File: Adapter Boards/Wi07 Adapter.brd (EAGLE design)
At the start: 25.4 x 24.1 mm, 5 parts, among them U1 WI07-12FULL

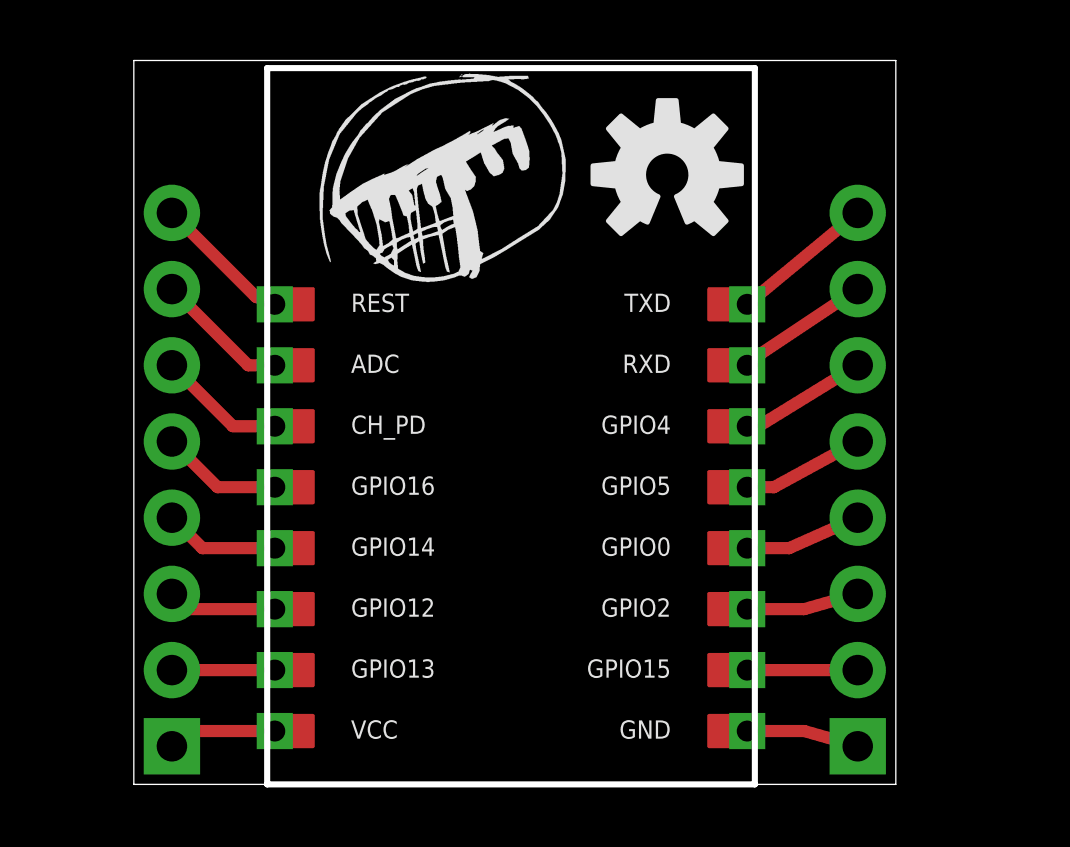
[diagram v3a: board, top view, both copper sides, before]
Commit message: Micronise hark logo; add multiple sizes
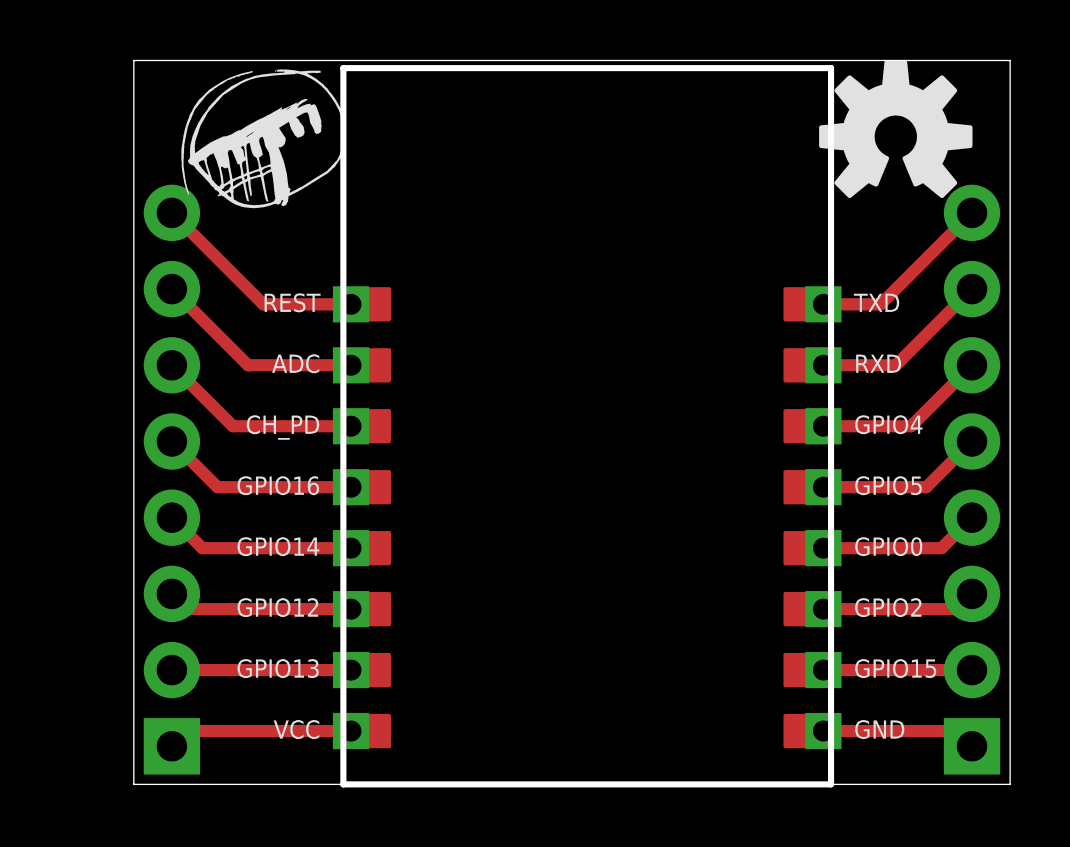
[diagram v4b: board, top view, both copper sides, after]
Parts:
- removed E$1: (no value), ESP:HARK
- added U$2: (no value), ESP:HARK-S
- moved U$1 7.73 mm to (25.4, 21.6)
- moved JP2 3.81 mm to (27.9, 1.27)
- moved U1 2.54 mm to (6.99, 0.00)
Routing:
- net N$8: track 4.64 -> 7.23 mm
- net N$3: track 3.64 -> 6.18 mm
- net N$1: track 3.64 -> 6.18 mm
- net N$7: track 4.48 -> 7.02 mm
- net N$6: track 4.27 -> 6.81 mm
- net N$5: track 4.06 -> 6.60 mm
- net N$4: track 3.85 -> 6.39 mm
- net N$2: track 3.43 -> 5.97 mm
- net N$11: track 4.26 -> 5.79 mm
- net N$12: track 4.07 -> 5.58 mm
- net N$13: track 3.90 -> 5.37 mm
- net N$9: track 4.78 -> 6.22 mm
- net N$16: track 3.75 -> 5.16 mm
- net N$14: track 3.75 -> 5.16 mm
- net N$10: track 4.71 -> 6.01 mm
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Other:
- board size 25.4 x 24.1 mm -> 29.2 x 24.1 mm
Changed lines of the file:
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@@
 <board>
 <plain>
-<wire x1="0" y1="0" x2="25.4" y2="0" width="0" layer="20"/>
-<wire x1="25.4" y1="0" x2="25.4" y2="24.13" width="0" layer="20"/>
-<wire x1="25.4" y1="24.13" x2="0" y2="24.13" width="0" layer="20"/>
+<wire x1="0" y1="0" x2="29.21" y2="0" width="0" layer="20"/>
+<wire x1="29.21" y1="0" x2="29.21" y2="24.13" width="0" layer="20"/>
+<wire x1="29.21" y1="24.13" x2="0" y2="24.13" width="0" layer="20"/>
 <wire x1="0" y1="24.13" x2="0" y2="0" width="0" layer="20"/>
 </plain>
@@
 <attribute name="VALUE" x="4.445" y="0" size="1.27" layer="27" rot="R90"/>
 </element>
-<element name="JP2" library="SparkFun-Connectors" package="1X08_PIN1_NO_SILK" value="" x="24.13" y="1.27" smashed="yes" rot="R90">
-<attribute name="NAME" x="22.3012" y="-0.0762" size="1.27" layer="27" ratio="10" rot="R90"/>
-<attribute name="VALUE" x="27.305" y="0" size="1.27" layer="27" rot="R90"/>
+<element name="JP2" library="SparkFun-Connectors" package="1X08_PIN1_NO_SILK" value="" x="27.94" y="1.27" smashed="yes" rot="R90">
+<attribute name="NAME" x="26.1112" y="-0.0762" size="1.27" layer="27" ratio="10" rot="R90"/>
+<attribute name="VALUE" x="31.115" y="0" size="1.27" layer="27" rot="R90"/>
 </element>
-<element name="U1" library="ESP" package="WI07-12" value="WI07-12FULL" x="4.445" y="0"/>
-<element name="U$1" library="SparkFun-Aesthetics" package="OSHW-LOGO-M" value="" x="17.78" y="20.32"/>
-<element name="E$1" library="ESP" package="HARK" value="" x="5.715" y="16.51"/>
+<element name="U$1" library="SparkFun-Aesthetics" package="OSHW-LOGO-M" value="" x="25.4" y="21.59"/>
+<element name="U1" library="ESP" package="WI07-12" value="WI07-12FULL" x="6.985" y="0"/>
+<element name="U$2" library="ESP" package="HARK-S" value="" x="1.27" y="19.05"/>
 </elements>
 <signals>
@@
 <contactref element="JP1" pad="1"/>
 <contactref element="U1" pad="VCC"/>
-<wire x1="4.699" y1="1.778" x2="1.778" y2="1.778" width="0.4064" layer="1"/>
+<wire x1="7.239" y1="1.778" x2="1.778" y2="1.778" width="0.4064" layer="1"/>
 <wire x1="1.778" y1="1.778" x2="1.27" y2="1.27" width="0.4064" layer="1"/>
 </signal>
@@
 <contactref element="JP1" pad="2"/>
 <contactref element="U1" pad="GPIO13"/>
-<wire x1="4.699" y1="3.81" x2="1.27" y2="3.81" width="0.4064" layer="1"/>
+<wire x1="7.239" y1="3.81" x2="1.27" y2="3.81" width="0.4064" layer="1"/>
 </signal>
 <signal name="N$3">
 <contactref element="JP1" pad="3"/>
 <contactref element="U1" pad="GPIO12"/>
-<wire x1="4.699" y1="5.842" x2="1.778" y2="5.842" width="0.4064" layer="1"/>
+<wire x1="7.239" y1="5.842" x2="1.778" y2="5.842" width="0.4064" layer="1"/>
 <wire x1="1.778" y1="5.842" x2="1.27" y2="6.35" width="0.4064" layer="1"/>
 </signal>
@@
 <contactref element="JP1" pad="4"/>
 <contactref element="U1" pad="GPIO14"/>
-<wire x1="4.699" y1="7.874" x2="2.286" y2="7.874" width="0.4064" layer="1"/>
+<wire x1="7.239" y1="7.874" x2="2.286" y2="7.874" width="0.4064" layer="1"/>
 <wire x1="2.286" y1="7.874" x2="1.27" y2="8.89" width="0.4064" layer="1"/>
 </signal>
@@
 <contactref element="JP1" pad="5"/>
 <contactref element="U1" pad="GPIO16"/>
-<wire x1="4.699" y1="9.906" x2="2.794" y2="9.906" width="0.4064" layer="1"/>
+<wire x1="7.239" y1="9.906" x2="2.794" y2="9.906" width="0.4064" layer="1"/>
 <wire x1="2.794" y1="9.906" x2="1.27" y2="11.43" width="0.4064" layer="1"/>
 </signal>
@@
 <contactref element="JP1" pad="6"/>
 <contactref element="U1" pad="CH_PD"/>
-<wire x1="4.699" y1="11.938" x2="3.302" y2="11.938" width="0.4064" layer="1"/>
+<wire x1="7.239" y1="11.938" x2="3.302" y2="11.938" width="0.4064" layer="1"/>
 <wire x1="3.302" y1="11.938" x2="1.27" y2="13.97" width="0.4064" layer="1"/>
 </signal>
@@
 <contactref element="JP1" pad="7"/>
 <contactref element="U1" pad="ADC"/>
-<wire x1="4.699" y1="13.97" x2="3.81" y2="13.97" width="0.4064" layer="1"/>
+<wire x1="7.239" y1="13.97" x2="3.81" y2="13.97" width="0.4064" layer="1"/>
 <wire x1="3.81" y1="13.97" x2="1.27" y2="16.51" width="0.4064" layer="1"/>
 </signal>
@@
 <contactref element="JP1" pad="8"/>
 <contactref element="U1" pad="REST"/>
-<wire x1="4.699" y1="16.002" x2="4.064" y2="16.256" width="0.4064" layer="1"/>
-<wire x1="4.064" y1="16.256" x2="1.27" y2="19.05" width="0.4064" layer="1"/>
+<wire x1="7.239" y1="16.002" x2="4.318" y2="16.002" width="0.4064" layer="1"/>
+<wire x1="4.318" y1="16.002" x2="1.27" y2="19.05" width="0.4064" layer="1"/>
 </signal>
 <signal name="N$9">
 <contactref element="JP2" pad="8"/>
 <contactref element="U1" pad="TXD"/>
-<wire x1="20.447" y1="16.002" x2="24.13" y2="19.05" width="0.4064" layer="1"/>
+<wire x1="22.987" y1="16.002" x2="24.892" y2="16.002" width="0.4064" layer="1"/>
+<wire x1="24.892" y1="16.002" x2="27.94" y2="19.05" width="0.4064" layer="1"/>
 </signal>
 <signal name="N$10">
 <contactref element="JP2" pad="7"/>
 <contactref element="U1" pad="RXD"/>
-<wire x1="20.447" y1="13.97" x2="20.32" y2="13.97" width="0.4064" layer="1"/>
-<wire x1="20.32" y1="13.97" x2="24.13" y2="16.51" width="0.4064" layer="1"/>
+<wire x1="22.987" y1="13.97" x2="25.4" y2="13.97" width="0.4064" layer="1"/>
+<wire x1="25.4" y1="13.97" x2="27.94" y2="16.51" width="0.4064" layer="1"/>
 </signal>
 <signal name="N$11">
 <contactref element="JP2" pad="6"/>
 <contactref element="U1" pad="GPIO4"/>
-<wire x1="20.447" y1="11.938" x2="20.828" y2="11.938" width="0.4064" layer="1"/>
-<wire x1="20.828" y1="11.938" x2="24.13" y2="13.97" width="0.4064" layer="1"/>
+<wire x1="22.987" y1="11.938" x2="25.908" y2="11.938" width="0.4064" layer="1"/>
+<wire x1="25.908" y1="11.938" x2="27.94" y2="13.97" width="0.4064" layer="1"/>
 </signal>
 <signal name="N$12">
 <contactref element="JP2" pad="5"/>
 <contactref element="U1" pad="GPIO5"/>
-<wire x1="20.447" y1="9.906" x2="21.336" y2="9.906" width="0.4064" layer="1"/>
-<wire x1="21.336" y1="9.906" x2="24.13" y2="11.43" width="0.4064" layer="1"/>
+<wire x1="22.987" y1="9.906" x2="26.416" y2="9.906" width="0.4064" layer="1"/>
+<wire x1="26.416" y1="9.906" x2="27.94" y2="11.43" width="0.4064" layer="1"/>
 </signal>
 <signal name="N$13">
 <contactref element="JP2" pad="4"/>
 <contactref element="U1" pad="GPIO0"/>
-<wire x1="20.447" y1="7.874" x2="21.844" y2="7.874" width="0.4064" layer="1"/>
-<wire x1="21.844" y1="7.874" x2="24.13" y2="8.89" width="0.4064" layer="1"/>
+<wire x1="22.987" y1="7.874" x2="26.924" y2="7.874" width="0.4064" layer="1"/>
+<wire x1="26.924" y1="7.874" x2="27.94" y2="8.89" width="0.4064" layer="1"/>
 </signal>
 <signal name="N$14">
 <contactref element="JP2" pad="3"/>
 <contactref element="U1" pad="GPIO2"/>
-<wire x1="20.447" y1="5.842" x2="22.352" y2="5.842" width="0.4064" layer="1"/>
-<wire x1="22.352" y1="5.842" x2="24.13" y2="6.35" width="0.4064" layer="1"/>
+<wire x1="22.987" y1="5.842" x2="27.432" y2="5.842" width="0.4064" layer="1"/>
+<wire x1="27.432" y1="5.842" x2="27.94" y2="6.35" width="0.4064" layer="1"/>
 </signal>
 <signal name="N$15">
 <contactref element="JP2" pad="2"/>
 <contactref element="U1" pad="GPIO15"/>
-<wire x1="20.447" y1="3.81" x2="24.13" y2="3.81" width="0.4064" layer="1"/>
+<wire x1="22.987" y1="3.81" x2="27.94" y2="3.81" width="0.4064" layer="1"/>
 </signal>
 <signal name="N$16">
 <contactref element="JP2" pad="1"/>
 <contactref element="U1" pad="GND"/>
-<wire x1="20.447" y1="1.778" x2="22.352" y2="1.778" width="0.4064" layer="1"/>
-<wire x1="22.352" y1="1.778" x2="24.13" y2="1.27" width="0.4064" layer="1"/>
+<wire x1="22.987" y1="1.778" x2="27.432" y2="1.778" width="0.4064" layer="1"/>
+<wire x1="27.432" y1="1.778" x2="27.94" y2="1.27" width="0.4064" layer="1"/>
 </signal>
 </signals>
